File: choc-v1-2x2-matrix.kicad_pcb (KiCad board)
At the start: 2 copper layers, 24 parts, among them SW1 SW_Push, U1 ATmega32U4-A, Y1 Crystal_GND24_Small

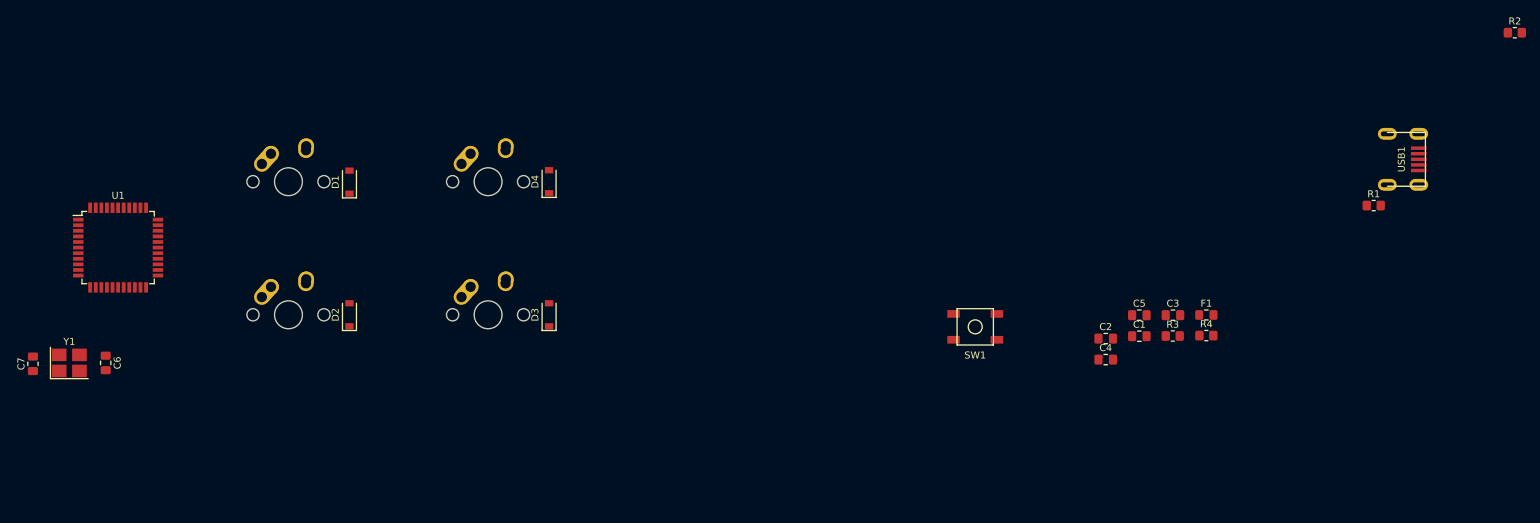
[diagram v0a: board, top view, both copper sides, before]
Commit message: still working on the footprint placement
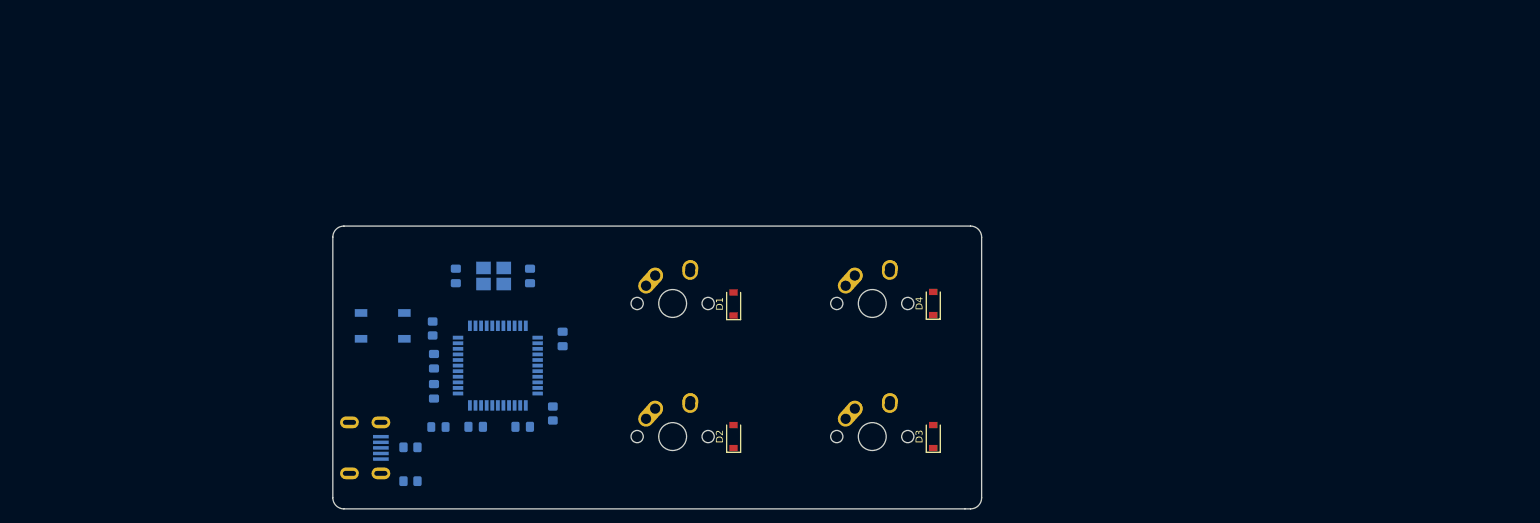
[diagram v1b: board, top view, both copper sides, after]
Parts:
- C1, C2, C3, C4, C5, C6, C7, F1, R1, R2, R3, R4, SW1, U1, USB1, Y1: moved to B.Cu
- moved R2 168.9 mm to (109.5, 107.1), turned to 180 degrees
- moved USB1 154.2 mm to (100.8, 107.2)
- moved R1 143.4 mm to (109.5, 111.9)
- moved F1 111.1 mm to (113.5, 104.2)
- moved C3 106.3 mm to (112.9, 99.1), turned to 90 degrees
- moved R3 105.9 mm to (112.7, 90.1), turned to 90 degrees
- moved C5 98.0 mm to (116.0, 82.5), turned to -90 degrees
- moved R4 94.2 mm to (129.9, 102.2), turned to -90 degrees
- moved C4 90.7 mm to (118.9, 104.1)
- moved SW1 84.8 mm to (105.6, 89.7), turned to 180 degrees
- moved C2 84.4 mm to (125.6, 104.1), turned to 180 degrees
- moved C1 82.6 mm to (131.3, 91.6), turned to 90 degrees
- moved C6 62.0 mm to (126.7, 82.5), turned to 90 degrees
- moved Y1 62.0 mm to (121.4, 82.5)
- moved D3 57.7 mm to (184.4, 105.5)
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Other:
- board outline added: 92.9 x 40.5 mm

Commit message: night 2
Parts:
- moved SW1 1.41 mm to (104.6, 88.7)
- moved R3 0.38 mm to (112.7, 89.7)
- moved C7 0.30 mm to (112.9, 94.5)
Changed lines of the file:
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@@
   )
   (setup
+    (stackup
+      (layer "F.SilkS" (type "Top Silk Screen"))
+      (layer "F.Paste" (type "Top Solder Paste"))
+      (layer "F.Mask" (type "Top Solder Mask") (thickness 0.01))
+      (layer "F.Cu" (type "copper") (thickness 0.035))
+      (layer "dielectric 1" (type "core") (thickness 1.51) (material "FR4") (epsilon_r 4.5) (loss_tangent 0.02))
+      (layer "B.Cu" (type "copper") (thickness 0.035))
+      (layer "B.Mask" (type "Bottom Solder Mask") (thickness 0.01))
+      (layer "B.Paste" (type "Bottom Solder Paste"))
+      (layer "B.SilkS" (type "Bottom Silk Screen"))
+      (copper_finish "None")
+      (dielectric_constraints no)
+    )
     (pad_to_mask_clearance 0)
     (pcbplotparams
@@
   )
   (footprint "Capacitor_SMD:C_0805_2012Metric_Pad1.18x1.45mm_HandSolder" (layer "B.Cu")
-    (at 112.903 99.06 90)
+    (at 112.903 99.04375 90)
     (descr "Capacitor SMD 0805 (2012 Metric), square (rectangular) end terminal, IPC_7351 nominal with elongated pad for handsoldering. (Body size source: IPC-SM-782 page 76, https://www.pcb-3d.com/wordpress/wp-content/uploads/ipc-sm-782a_amendment_1_and_2.pdf, https://docs.google.com/spreadsheets/d/1BsfQQcO9C6DZCsRaXUlFlo91Tg2WpOkGARC1WS5S8t0/edit?usp=sharing), generated with kicad-footprint-generator")
     (tags "capacitor handsolder")
@@
   )
   (footprint "Resistor_SMD:R_0805_2012Metric_Pad1.20x1.40mm_HandSolder" (layer "B.Cu")
-    (at 112.7125 90.06875 90)
+    (at 112.7125 89.69375 90)
     (descr "Resistor SMD 0805 (2012 Metric), square (rectangular) end terminal, IPC_7351 nominal with elongated pad for handsoldering. (Body size source: IPC-SM-782 page 72, https://www.pcb-3d.com/wordpress/wp-content/uploads/ipc-sm-782a_amendment_1_and_2.pdf), generated with kicad-footprint-generator")
     (tags "resistor handsolder")
@@
   )
   (footprint "random-keyboard-parts:SKQG-1155865" (layer "B.Cu")
-    (at 105.56875 89.69375 180)
+    (at 104.56875 88.69375 180)
     (property "Sheetfile" "choc-v1-2x2-matrix.kicad_sch")
     (property "Sheetname" "")
@@
   )
   (footprint "Capacitor_SMD:C_0805_2012Metric_Pad1.18x1.45mm_HandSolder" (layer "B.Cu")
-    (at 112.903 94.75225 90)
+    (at 112.903 94.45625 90)
     (descr "Capacitor SMD 0805 (2012 Metric), square (rectangular) end terminal, IPC_7351 nominal with elongated pad for handsoldering. (Body size source: IPC-SM-782 page 76, https://www.pcb-3d.com/wordpress/wp-content/uploads/ipc-sm-782a_amendment_1_and_2.pdf, https://docs.google.com/spreadsheets/d/1BsfQQcO9C6DZCsRaXUlFlo91Tg2WpOkGARC1WS5S8t0/edit?usp=sharing), generated with kicad-footprint-generator")
     (tags "capacitor handsolder")
